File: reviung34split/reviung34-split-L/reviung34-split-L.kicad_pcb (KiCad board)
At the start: 2 copper layers, 100 x 100 mm, 47 parts, among them J1 8P8C, SW1 SW_PUSH, SW10 SW_PUSH, SW11 SW_PUSH, SW12 SW_PUSH, SW13 SW_PUSH, SW14 SW_PUSH, SW15 SW_PUSH, SW16 SW_PUSH, SW17 SW_PUSH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

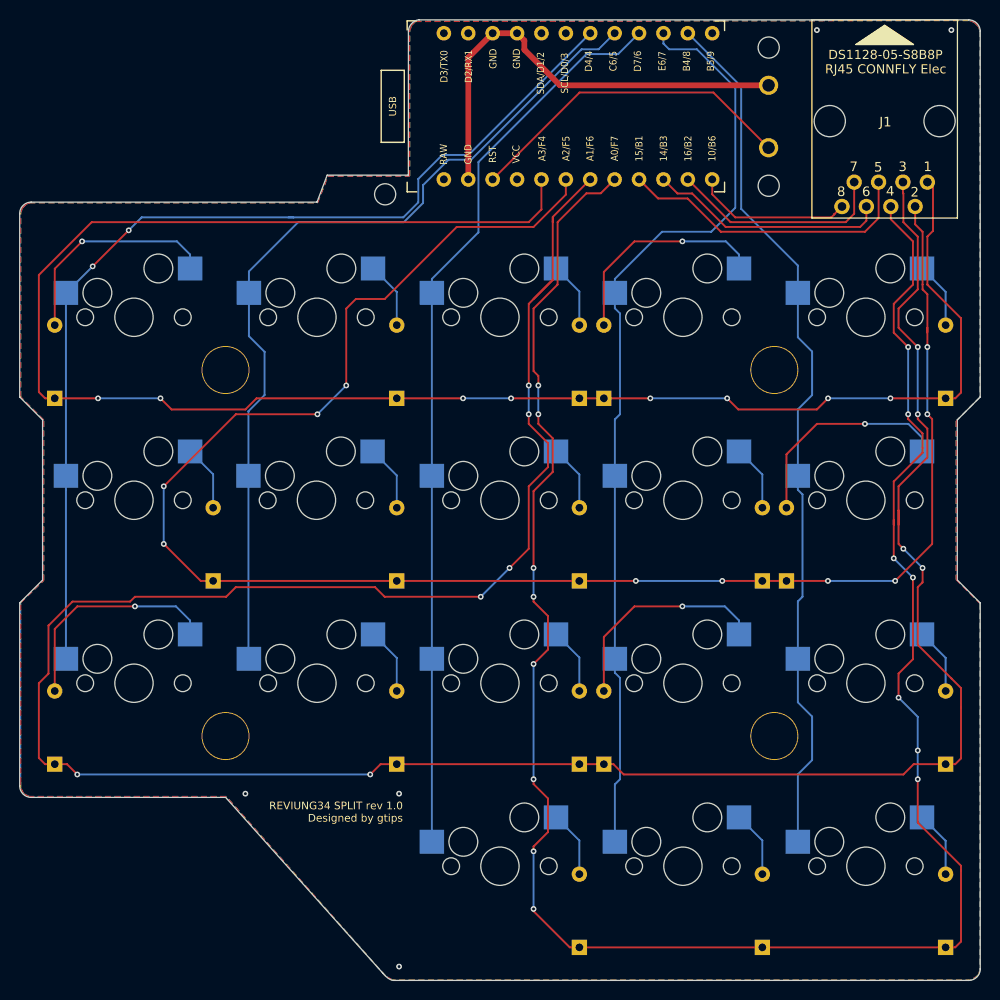
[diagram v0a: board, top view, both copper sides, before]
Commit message: RJ45_NONAME_8P8C_Horizontal
Redone with very common RJ45_NONAME_8P8C_Horizontal socket's footprint and KiCad 6.0.4.
https://aliexpress.ru/item/32774556179.html
https://aliexpress.ru/item/4001295248605.html
https://aliexpress.ru/item/32694863099.html
https://aliexpress.ru/item/32902228456.html
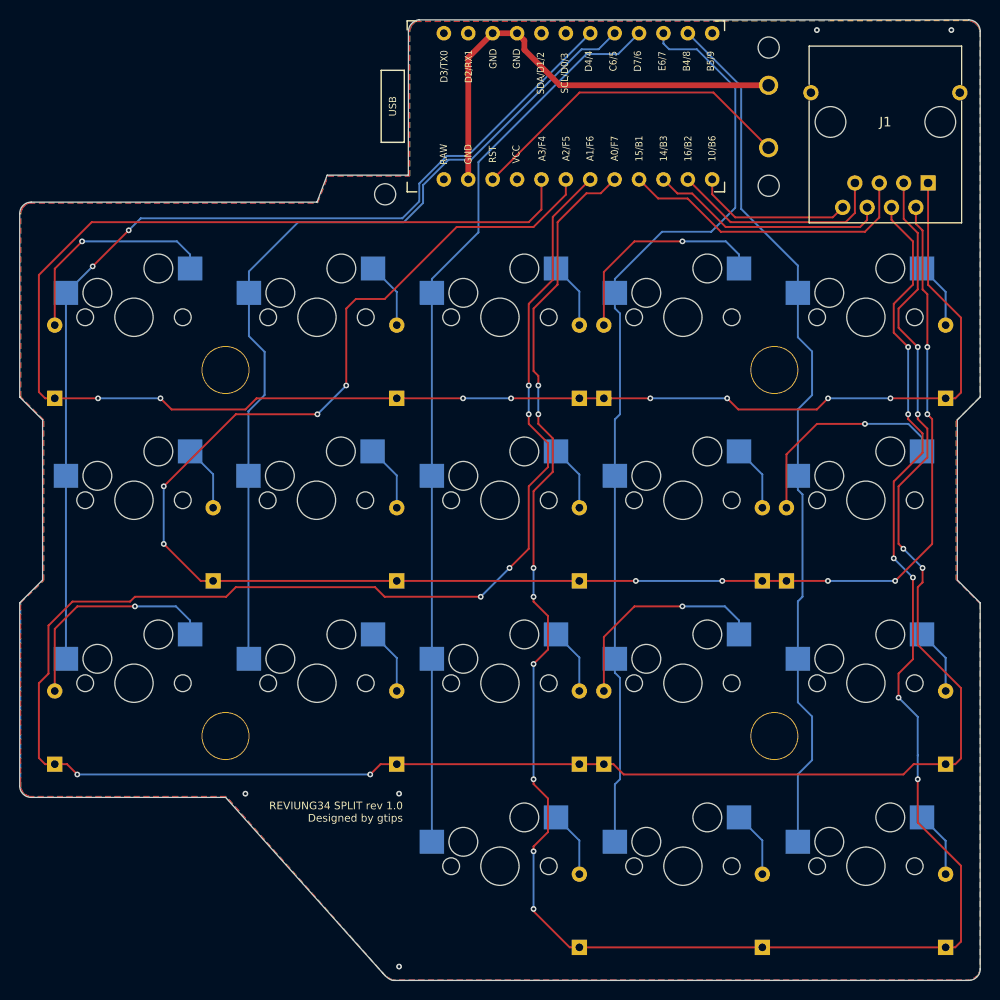
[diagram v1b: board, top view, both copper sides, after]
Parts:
- J1: footprint _reviung-kbd:RJ45-DS1128-05-S8B8P -> Connector_NONAME:RJ45_NONAME_8P8C_Horizontal
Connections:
- U1 pad 1: Net-(U1-Pad1) -> unconnected-(U1-Pad1)
- U1 pad 12: Net-(U1-Pad12) -> unconnected-(U1-Pad12)
- U1 pad 2: Net-(U1-Pad2) -> unconnected-(U1-Pad2)
- U1 pad 24: Net-(U1-Pad24) -> unconnected-(U1-Pad24)
- U1 pad 5: Net-(U1-Pad5) -> unconnected-(U1-Pad5)
- U1 pad 6: Net-(U1-Pad6) -> unconnected-(U1-Pad6)
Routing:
- net row2: track 281.3 -> 276.3 mm
- net col0: track 105.8 -> 105.0 mm
- net row1: track 186.3 -> 185.6 mm
- net row3: track 216.4 -> 215.8 mm, vias 15 -> 14
- net row0: track 192.8 -> 192.1 mm
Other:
- net class Default removed
